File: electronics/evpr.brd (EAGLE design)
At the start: 97.2 x 41.3 mm, 127 parts, among them J1 10118193-0001LF, Q1 AOD4184A, Q2 AOD4184A, T3 MMBT2222A, T5 MMBT2222A, U1 BQ2057TTS, U3 ESP32-WROOM-32D, U6 SN74AHCT125DR, U7 TPSM84824MOLR, U8 LTC4353CMSPBFMSOP-16_MS-M, X1 B3P-VH(LF)(SN), X2 BM02B-PASS-1-TFT(LF)(SN), X3 BM03B-PASS-1-TFT(LF)(SN), X4 BM03B-PASS-1-TFT(LF)(SN), X5 BM04B-PASS-1-TFT(LF)(SN)

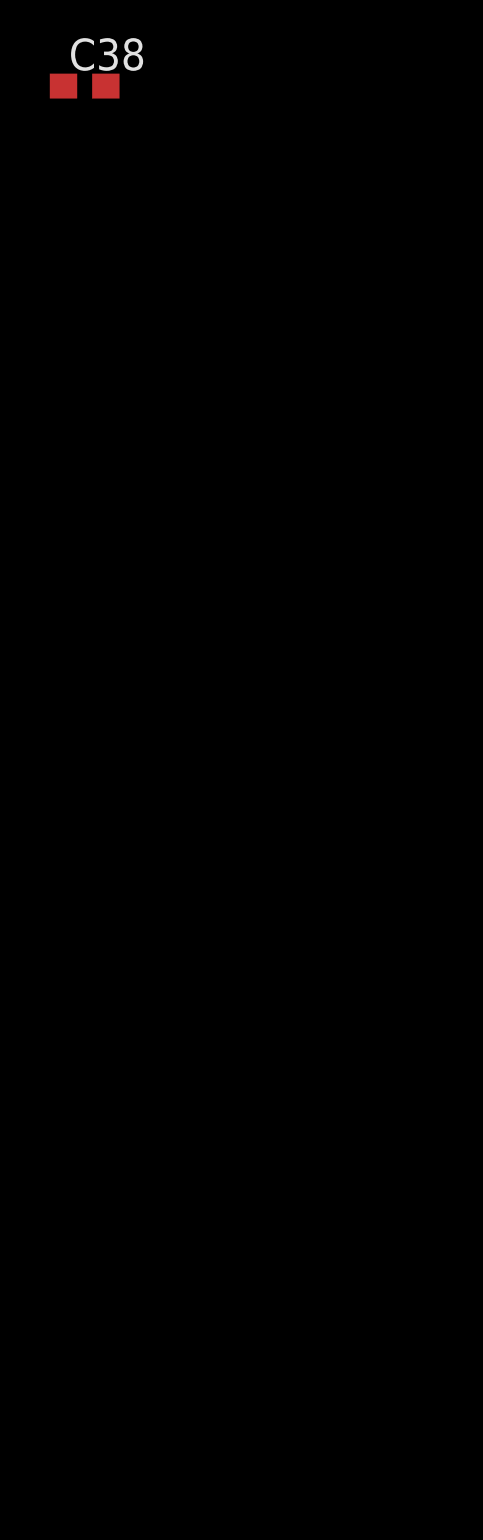
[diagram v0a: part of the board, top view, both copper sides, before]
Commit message: Added EMI Testing optionals
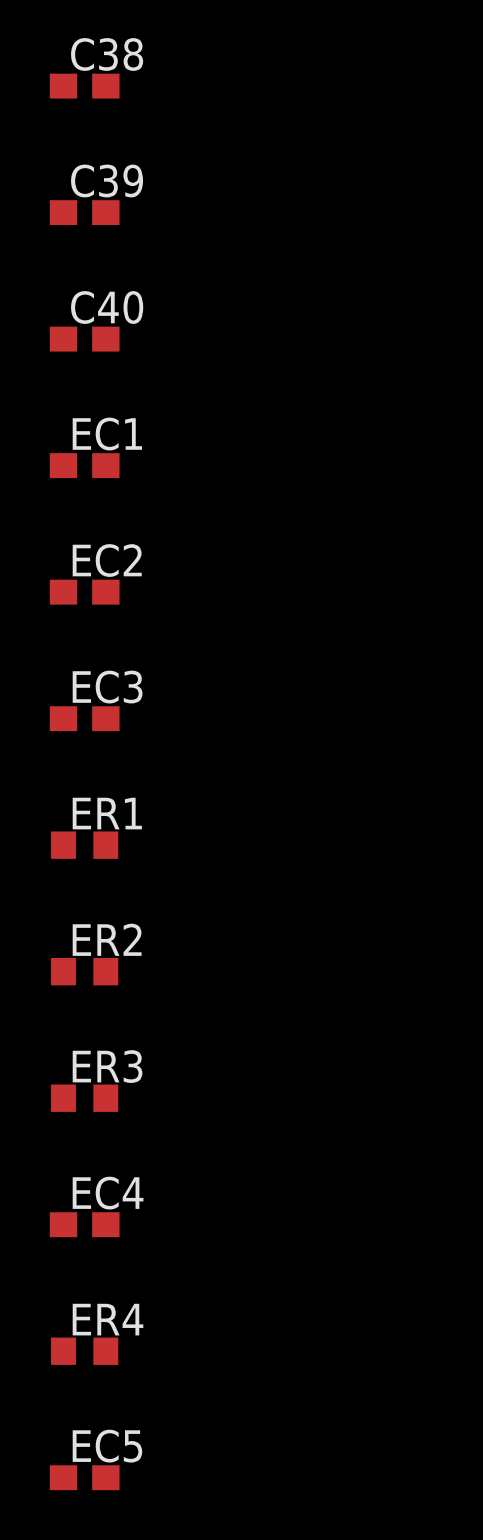
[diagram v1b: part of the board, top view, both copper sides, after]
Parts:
- added C39, C40, EC1, EC2, EC3, EC4, EC5: 0.1uF, eagle-ltspice:C0603
- added ER1, ER2, ER3, ER4: 0, rcl:R0603
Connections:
- new net N$11: ER1.1, X3.P$2
- new net N$12: ER2.1, X4.P$2
- new net N$30: ER3.1, X5.P$2
- new net N$42: ER4.1, X5.P$3
- net ESP_POWER: now also C39.2
- net GND: now also C39.1, C40.2, EC1.2, EC2.2, EC3.2, EC4.2, EC5.2
- net N$22: now also EC4.1, ER4.2; no longer X5.P$3
- net N$27: now also EC5.1, ER3.2; no longer X5.P$2
- net SERVO1: now also EC2.1, ER1.2; no longer X3.P$2
- net SERVO2: now also EC3.1, ER2.2; no longer X4.P$2
- net TACH: now also EC1.1
- net VRAW: now also C40.1

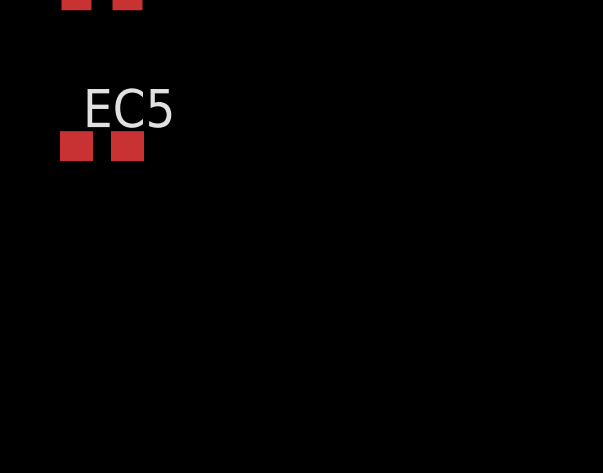
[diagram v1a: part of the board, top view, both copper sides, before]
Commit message: Added testpoints; Reviewed all testpoints; Corrected 3.3V converter to AP63203
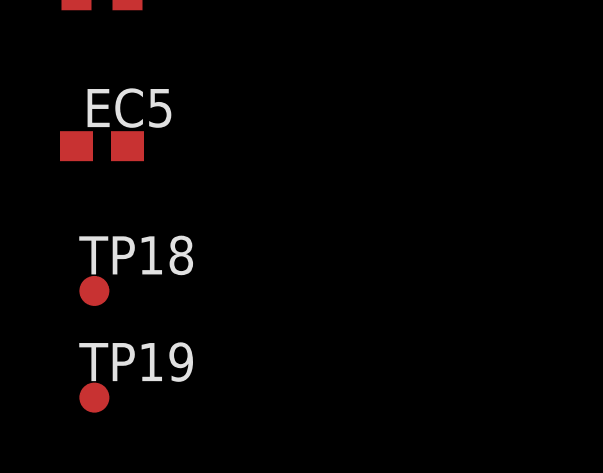
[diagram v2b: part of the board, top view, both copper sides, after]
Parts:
- added TP18, TP19: PTR1TP10R, testpad:TP10R
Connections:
- net N$34: now also TP18.TP
- net N$40: now also TP19.TP
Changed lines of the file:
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@@
 <attribute name="VALUE" x="-73.533" y="-390.779" size="1.27" layer="27"/>
+</element>
+<element name="TP18" library="testpad" library_urn="urn:adsk.eagle:library:385" package="TP10R" package3d_urn="urn:adsk.eagle:package:27959/1" value="PTR1TP10R" x="-73.152" y="-393.7" smashed="yes">
+<attribute name="NAME" x="-73.6521" y="-393.1501" size="1.27" layer="25"/>
+<attribute name="POPULARITY" value="0" x="-73.152" y="-393.7" size="1.778" layer="27" display="off"/>
+<attribute name="TP_SIGNAL_NAME" value="" x="-73.152" y="-393.7" size="1.778" layer="27" display="off"/>
+<attribute name="VALUE" x="-73.533" y="-394.208" size="0.0254" layer="27"/>
+</element>
+<element name="TP19" library="testpad" library_urn="urn:adsk.eagle:library:385" package="TP10R" package3d_urn="urn:adsk.eagle:package:27959/1" value="PTR1TP10R" x="-73.152" y="-397.256" smashed="yes">
+<attribute name="NAME" x="-73.6521" y="-396.7061" size="1.27" layer="25"/>
+<attribute name="POPULARITY" value="0" x="-73.152" y="-397.256" size="1.778" layer="27" display="off"/>
+<attribute name="TP_SIGNAL_NAME" value="" x="-73.152" y="-397.256" size="1.778" layer="27" display="off"/>
+<attribute name="VALUE" x="-73.533" y="-397.764" size="0.0254" layer="27"/>
 </element>
 </elements>
@@
 <wire x1="41.654" y1="-16.002" x2="41.654" y2="-18.352" width="0.254" layer="16"/>
 <wire x1="41.654" y1="-18.352" x2="41.554" y2="-18.452" width="0.254" layer="16"/>
+<contactref element="TP18" pad="TP"/>
+<wire x1="41.656" y1="-21.121" x2="-73.152" y2="-393.7" width="0" layer="19" extent="1-16"/>
 </signal>
 <signal name="N$29">
@@
 <contactref element="C16" pad="2"/>
 <contactref element="C22" pad="2"/>
+<contactref element="TP19" pad="TP"/>
+<wire x1="-61.126" y1="-70.358" x2="-73.152" y2="-397.256" width="0" layer="19" extent="1-1"/>
 <wire x1="-61.126" y1="-65.278" x2="-61.126" y2="-70.358" width="0" layer="19" extent="1-1"/>
 <wire x1="33.635" y1="-29.546" x2="-61.126" y2="-65.278" width="0" layer="19" extent="1-16"/>

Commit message: Update all component names to follow new standard naming system
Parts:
- renumbered C1 to C.M1, C10 to C.M10, C11 to C.Z11, C12 to C.F12, C13 to C.B13, C14 to C.Z14, C15 to C.F15, C16 to C.P16, C17 to C.F17, C18 to C.Z18, C19 to C.Z19, C2 to C.M2, C20 to C.F20, C21 to C.D21, C22 to C.P22, C23 to C.P23, C24 to C.P24, C25 to C.Z25, C26 to C.F26, C27 to C.J27, C28 to C.J28, C29 to C.M29, C3 to C.M3, C30 to C.L30, C31 to C.L31, C32 to C.B32, C33 to C.Y33, C34 to C.Z34, C35 to C.F35, C36 to C.F36, C37 to C.S37, C38 to C.S38, C39 to C.G39, C4 to C.M4, C40 to C.M40, C5 to C.M5, C6 to C.Y6, C7 to C.Y7, C8 to C.Y8, C9 to C.F9, EC1 to C.EJ1, EC2 to C.ES2, EC3 to C.ES3, EC4 to R.CD4, EC5 to R.CD5, ER1 to R.ES1, ER2 to R.ES2, ER3 to R.ED3, ER4 to R.ED4, F1 to F.D1, J1 to X.F1, LED1 to D.J1, LED2 to L.P2, LED3 to D.F3, Q1 to Q.Y1, Q2 to Q.Y2, R1 to R.M1, R10 to R.G10, R11 to R.M11, R12 to R.P12, R13 to R.P13, R14 to R.P14, R15 to R.J15, R16 to R.P16, R17 to R.F17, R18 to R.F18, R19 to R.F19, R20 to R.J20, R21 to R.J21, R22 to R.J22, R23 to R.J23, R24 to R.L24, R25 to R.L25, R26 to R.L26, R27 to R.L27, R28 to R.K28, R3 to R.B3, R30 to R.F30, R32 to R.M32, R33 to R.L33, R34 to R.L34, R4 to R.B4, R5 to R.B5, R6 to R.B6, R7 to R.Y7, R8 to R.M8, R9 to R.K9, SJ2 to SJ.K2, SV5 to X.G1, T3 to T.P3, T5 to T.P5, TP1 to TP.Y1, TP10 to TP.F10, TP11 to TP.F11, TP12 to TP.Z12, TP13 to TP.P13, TP14 to TP.P14, TP15 to TP.P15, TP16 to TP.P16, TP17 to TP.Z17, TP18 to TP.F18, TP19 to TP.P19, TP2 to TP.J2, TP3 to TP.J3, TP4 to TP.L4, TP5 to TP.M5, TP6 to TP.B6, TP7 to TP.M7, TP8 to TP.L8, TP9 to TP.F9, U$1 to X.K1, U$10 to Q.Z10, U$11 to Q.L11, U$12 to U.P12, U$13 to Q.Z13, U$15 to C.D15, U$16 to Q.J16, U$17 to U.Z17, U$19 to L.Z19, U$2 to U.F2, U$20 to L.F20, U$3 to Q.B3, U$4 to Q.K4, U$5 to Q.L5, U$6 to Q.F6, U$7 to Q.F7, U$8 to Q.Z8, U$9 to Q.L9, U1 to U.B1, U3 to U.G3, U6 to U.D6, U8 to U.Y8, X1 to X.J1, X2 to X.S2, X3 to X.S3, X4 to X.S4, X5 to X.D5, XA1 to X.L1, XA2 to X.L2

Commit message: Hacked USB profile to have wires on internal layers. Seems to make Eagle behave.
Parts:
- removed C.ES3: 0.1uF, eagle-ltspice:C0603
- removed R.B5, R.B6: 100k, rcl:R0603
- removed TP.J3: PTR1TP10R, testpad:TP10R
- removed X.S4: BM03B-PASS-1-TFT(LF)(SN), mccloud:BM03B-PASS-1-TFT(LF)(SN)
- added C.ES1: 0.1uF, eagle-ltspice:C0603
- added R.B1: 0.25, rcl:R0603
- added R.B2: 1k, rcl:R0603
- added TP.J1: PTR1TP10R, testpad:TP10R
- added X.S1: BM02B-PASS-1-TFT(LF)(SN), mccloud:BM02B-PASS-1-TFT(LF)(SN)
- R.B3: value 0.25 -> 100k
- R.B4: value 1k -> 100k
- X.S2: value BM02B-PASS-1-TFT(LF)(SN) -> BM03B-PASS-1-TFT(LF)(SN); device mccloud:BM02B-PASS-1-TFT(LF)(SN) -> mccloud:BM03B-PASS-1-TFT(LF)(SN)
- moved X.S3 270.1 mm to (75.9, -27.9)
- moved X.S2 11.2 mm to (-68.3, -256.3)
- moved R.B4 7.43 mm to (-12.9, -45.8), flipped to the bottom, turned to 270 degrees
- moved TP.J2 6.94 mm to (-24.9, -40.6), flipped to the top, turned to 90 degrees
- moved C.ES2 5.08 mm to (-72.9, -358.4)
- moved R.B3 1.73 mm to (-16.5, -45.8), flipped to the bottom, turned to 0 degrees
- renumbered C.B13 to C.B1, C.B32 to C.B2, C.D15 to C.D1, C.D21 to C.D2, C.F12 to C.F2, C.F15 to C.F3, C.F17 to C.F4, C.F20 to C.F5, C.F26 to C.F6, C.F35 to C.F7, C.F36 to C.F8, C.F9 to C.F1, C.G39 to C.G1, C.J27 to C.J1, C.J28 to C.J2, C.L30 to C.L1, C.L31 to C.L2, C.M10 to C.M6, C.M29 to C.M7, C.M40 to C.M8, C.P16 to C.P1, C.P22 to C.P2, C.P23 to C.P3, C.P24 to C.P4, C.S37 to C.S1, C.S38 to C.S2, C.Y33 to C.Y4, C.Y6 to C.Y1, C.Y7 to C.Y2, C.Y8 to C.Y3, C.Z11 to C.Z1, C.Z14 to C.Z2, C.Z18 to C.Z3, C.Z19 to C.Z4, C.Z25 to C.Z5, C.Z34 to C.Z6, D.F3 to D.F1, L.F20 to L.F1, L.P2 to L.P1, L.Z19 to L.Z1, Q.B3 to Q.B1, Q.F6 to Q.F1, Q.F7 to Q.F2, Q.J16 to Q.J1, Q.K4 to Q.K1, Q.L11 to Q.L3, Q.L5 to Q.L1, Q.L9 to Q.L2, Q.Z10 to Q.Z2, Q.Z13 to Q.Z3, Q.Z8 to Q.Z1, R.CD4 to R.CD1, R.CD5 to R.CD2, R.ED3 to R.ED1, R.ED4 to R.ED2, R.F17 to R.F1, R.F18 to R.F2, R.F19 to R.F3, R.F30 to R.F4, R.G10 to R.G1, R.J15 to R.J1, R.J20 to R.J2, R.J21 to R.J3, R.J22 to R.J4, R.J23 to R.J5, R.K28 to R.K2, R.K9 to R.K1, R.L24 to R.L1, R.L25 to R.L2, R.L26 to R.L3, R.L27 to R.L4, R.L33 to R.L5, R.L34 to R.L6, R.M11 to R.M3, R.M32 to R.M4, R.M8 to R.M2, R.P12 to R.P1, R.P13 to R.P2, R.P14 to R.P3, R.P16 to R.P4, R.Y7 to R.Y1, SJ.K2 to SJ.K1, T.P3 to T.P1, T.P5 to T.P2, TP.B6 to TP.B1, TP.F10 to TP.F2, TP.F11 to TP.F3, TP.F18 to TP.F4, TP.F9 to TP.F1, TP.L4 to TP.L1, TP.L8 to TP.L2, TP.M5 to TP.M1, TP.M7 to TP.M2, TP.P13 to TP.P1, TP.P14 to TP.P2, TP.P15 to TP.P3, TP.P16 to TP.P4, TP.P19 to TP.P5, TP.Z12 to TP.Z1, TP.Z17 to TP.Z2, U.D6 to U.D1, U.F2 to U.F1, U.G3 to U.G1, U.P12 to U.P1, U.Y8 to U.Y1, U.Z17 to U.Z1, U7 to U1, X.D5 to X.D1
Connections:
- net GND: now also C.ES1.2, R.B4.1, X.S1.P$1, X.S1.P$5, X.S1.P$6, X.S2.P$3; no longer C.ES3.2, R.B6.1, X.S2.P$1, X.S4.P$3, X.S4.P$5, X.S4.P$6
- net N$11: now also X.S2.P$2; no longer X.S3.P$2
- net N$12: now also X.S3.P$2; no longer X.S4.P$2
- net N$5: now also R.B1.2; no longer R.B3.2
- net N$6: now also R.B2.2; no longer R.B4.2
- net N$7: now also R.B3.1, R.B4.2; no longer R.B5.1, R.B6.2
- net N$9: now also R.B2.1; no longer R.B4.1
- net SERVO1: now also C.ES1.1; no longer C.ES2.1
- net SERVO2: now also C.ES2.1; no longer C.ES3.1
- net SYS_POWER: now also X.S1.P$2, X.S2.P$1; no longer X.S2.P$2, X.S4.P$1
- net TACH_RAW: now also TP.J1.TP; no longer TP.J2.TP
- net VRAW: now also R.B1.1, R.B3.2, TP.J2.TP; no longer R.B3.1, R.B5.2, TP.J3.TP

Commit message: Finished routing board. Wow.
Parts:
- removed C.B2, C.M8, C.S2: 0.1uF, eagle-ltspice:C0603
- removed D.F1, L.P1: (no value), led:CHIP-LED0805
- removed R.F1: 250Ω, rcl:R0603
- removed U1: TPSM84824MOLR, mccloud:MOL0024A
- added D.P1, D.Z1: (no value), led:CHIP-LED0805
- added R.P5: 250Ω, mccloud:R0603
- added U.M1: TPSM84824MOLR, mccloud:MOL0024A
- C.B1, C.D2, C.EJ1, C.ES1, C.ES2, C.F1, C.F2, C.F6, C.F7, C.F8, C.G1, C.J1, C.J2, C.L1, C.L2, C.M7, C.P1, C.P2, C.P3, C.P4, C.S1, C.Y1, C.Y2, C.Y3, C.Y4, C.Z3, C.Z5, C.Z6, R.CD1, R.CD2: device eagle-ltspice:C0603 -> mccloud:C0603
- C.F3, C.F4, C.F5, C.Z2, C.Z4: device rcl:C0603 -> mccloud:C0603
- C.Z1: device eagle-ltspice:C1210 -> mccloud:C0603
- R.B1, R.B2, R.B3, R.B4, R.ED1, R.ED2, R.ES1, R.ES2, R.F2, R.F3, R.F4, R.G1, R.J1, R.J2, R.J3, R.J4, R.J5, R.K1, R.K2, R.L1, R.L2, R.L3, R.L4, R.L5, R.L6, R.M1, R.M2, R.M3, R.M4, R.P1, R.P2, R.P3, R.P4, R.Y1: device rcl:R0603 -> mccloud:R0603
- moved TP.P5 387.5 mm to (30.7, -23.9)
- moved R.CD2 380.5 mm to (39.5, -25.4), flipped to the bottom, turned to 180 degrees
- moved TP.F4 379.1 mm to (45.2, -33.5)
- moved R.ED2 376.4 mm to (37.1, -23.8), turned to 180 degrees
- moved R.CD1 370.0 mm to (38.6, -25.9)
- moved R.ED1 367.9 mm to (39.6, -23.3), flipped to the bottom
- moved R.ES2 345.5 mm to (13.8, -34.1), turned to 120 degrees
- moved R.ES1 337.1 mm to (13.7, -37.6), turned to 300 degrees
- moved C.ES2 333.7 mm to (15.5, -36.7), turned to 300 degrees
- moved C.ES1 326.2 mm to (11.2, -38.1), turned to 300 degrees
- moved C.EJ1 324.8 mm to (-18.8, -27.9), flipped to the bottom, turned to 270 degrees
- moved C.F7 317.8 mm to (46.6, -23.3), turned to 90 degrees
- moved C.F8 314.9 mm to (46.9, -31.6), turned to 90 degrees
- moved C.G1 308.0 mm to (17.7, -43.7), turned to 120 degrees
- moved C.S1 306.2 mm to (8.64, -32.8), turned to 210 degrees
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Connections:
- removed net BUILTIN_LED: R.P4.2
- removed net N$25: D.F1.A, R.F1.1
- removed net SHUTDOWN: U.G1.13
- removed net SHUTDOWN_CANCEL: U.G1.9
- new net N$36: D.Z1.A, R.P5.1
- net 5.0V: no longer R.F1.2
- net AGND: now also U.M1.23, U.M1.3, U.M1.9; no longer U1.23, U1.3, U1.9
- net BATSENSE1: now also U.G1.5; no longer U.G1.4
- net BATSENSE2: now also U.G1.4; no longer U.G1.5
- net ESP_POWER: now also R.P5.2
- net GND: now also D.P1.C, D.Z1.C, U.M1.12, U.M1.13, U.M1.14, U.M1.15, U.M1.18, U.M1.19, U.M1.20, U.M1.21; no longer C.B2.2, C.M8.2, C.S2.1, D.F1.C, L.P1.C, U1.12, U1.13, U1.14, U1.15, U1.18, U1.19, U1.20, U1.21
- net LED_BUILTIN: now also R.P4.2
- net N$11: now also C.ES1.1
- net N$12: now also C.ES2.1
- net N$15: now also U.M1.16, U.M1.17; no longer U1.16, U1.17
- net N$17: now also U.M1.24; no longer U1.24
- net N$24: now also D.P1.A; no longer L.P1.A
- net N$3: now also U.M1.2; no longer U1.2
- net N$31: now also U.M1.5; no longer U1.5
- net POWERSAVE: now also U.G1.33; no longer U.G1.24
- net SERVO1: no longer C.ES1.1
- net SERVO2: no longer C.ES2.1
- net SYS_POWER: no longer C.S2.2
- net USBSENSE: now also U.G1.32; no longer U.G1.23
- net VBAT: no longer C.B2.1
- net VCONV: now also U.M1.1, U.M1.8; no longer U1.1, U1.8
- net VRAW: now also U.M1.11, U.M1.22; no longer C.M8.1, U1.11, U1.22
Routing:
- net RAWSENSE: track 27.6 -> 89.4 mm, vias 2 -> 4
- net SERVO2: track 60.2 -> 3.73 mm
- net VBAT: track 86.3 -> 132.7 mm, vias 11 -> 12
- net SYS_POW_EN: track 18.4 -> 61.4 mm, vias 2 -> 5
- net N$27: track 43.2 -> 4.42 mm, vias 2 -> 0
- net BATSENSE2: track 24.7 -> 63.2 mm, vias 2 -> 6
- net N$22: track 44.0 -> 6.08 mm
- net USING_ENG: track 42.0 -> 77.0 mm, vias 2 -> 5
- net POWERSAVE: track 50.0 -> 84.0 mm, vias 1 -> 5
- net TACH: track 83.3 -> 114.9 mm, vias 2 -> 6
- net CSTAT: track 47.8 -> 77.9 mm, vias 2 -> 5
- net VRAW: track 109.3 -> 81.1 mm, vias 11 -> 12
- net SYS_POWER: track 42.4 -> 70.3 mm, vias 18 -> 25
- net DS_DAT: track 3.73 -> 29.2 mm, vias 1 -> 2
- net BATSENSE1: track 25.3 -> 50.3 mm
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- added copper zone on layer 2, net AGND
- added copper zone on layer 2, net GND
- added copper zone on layer 1, net SYS_POWER
- added copper zone on layer 15, net SYS_POWER
- added copper zone on layer 1, net VBAT
- added copper zone on layer 16, net VBAT
- added copper zone on layer 1, net VCONV
- added copper zone on layer 16, net VCONV
- added copper zone on layer 16, net VRAW
- removed copper zone on layer 15, net GND
- removed copper zone on layer 2, net SYS_POWER
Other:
- board size 97.2 x 41.3 mm -> 88.3 x 47 mm

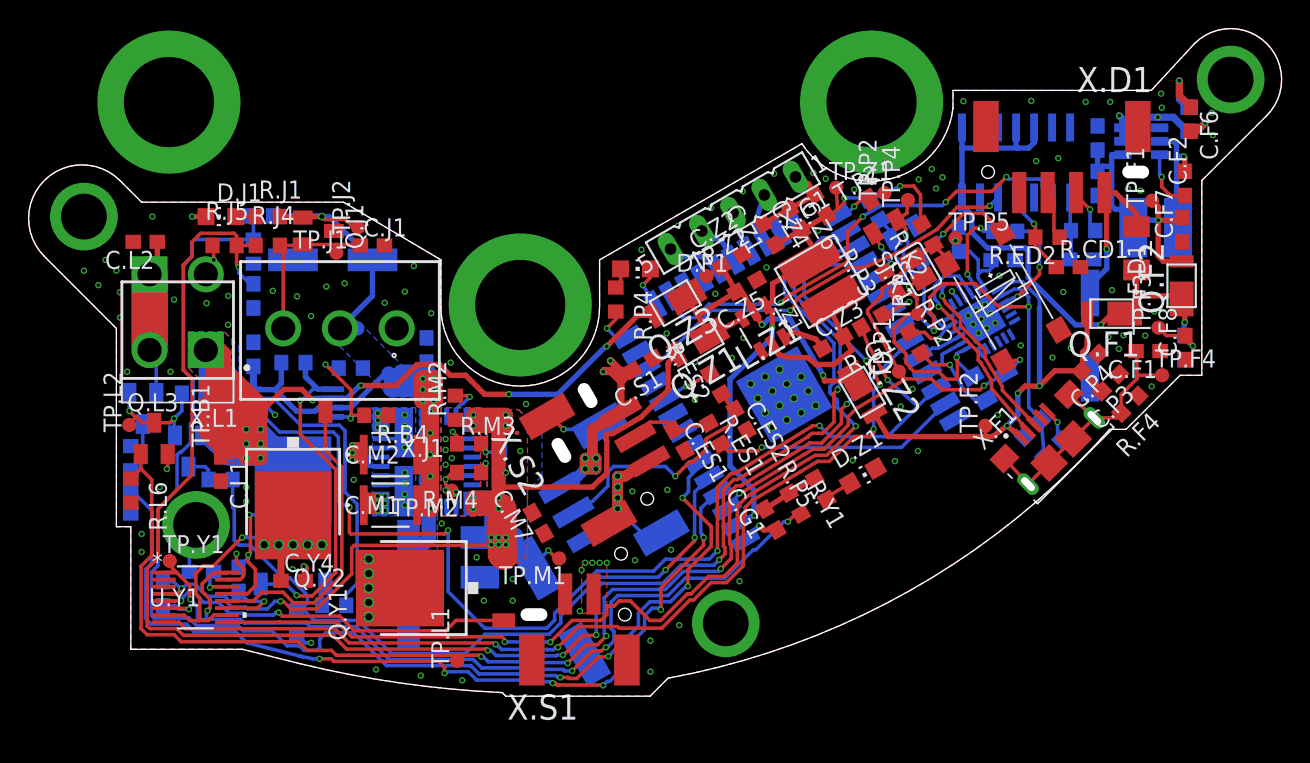
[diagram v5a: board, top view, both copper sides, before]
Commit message: Completed silkscreen alignment
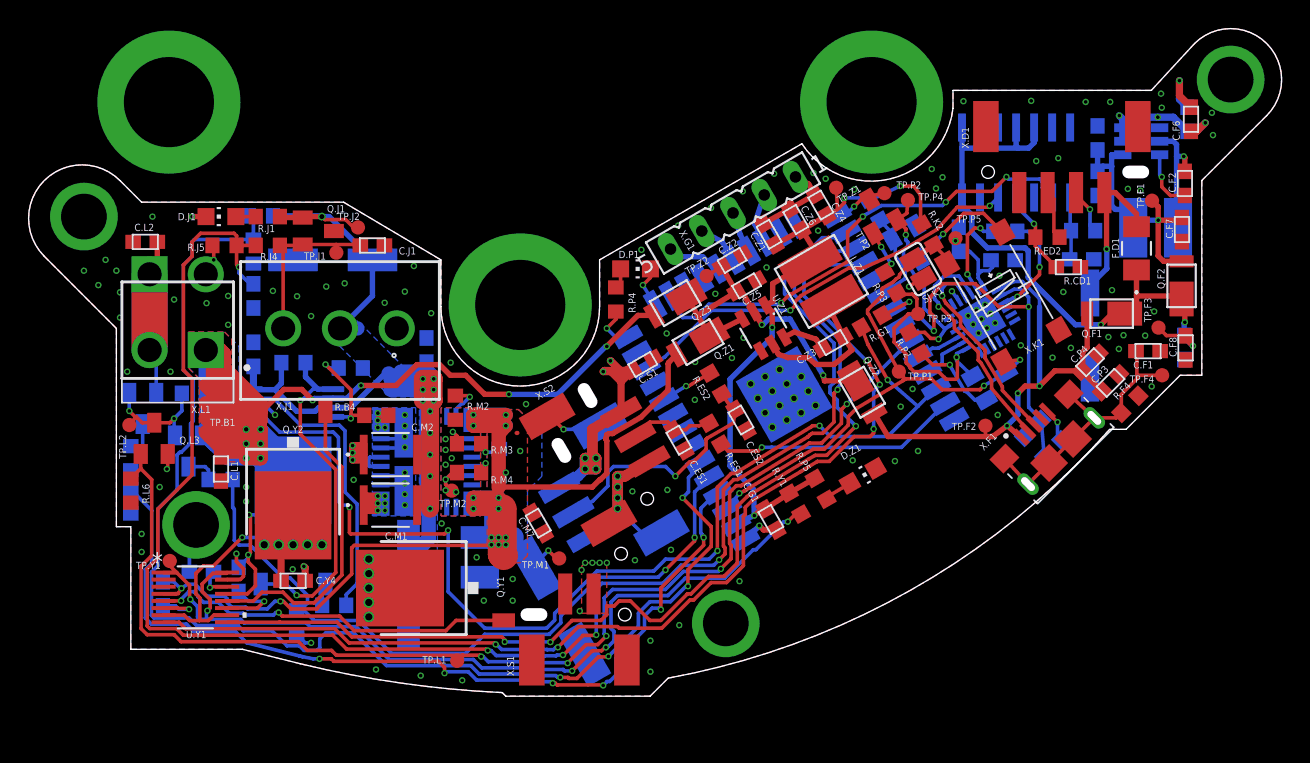
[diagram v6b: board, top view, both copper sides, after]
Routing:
- net GND: vias 165 -> 164

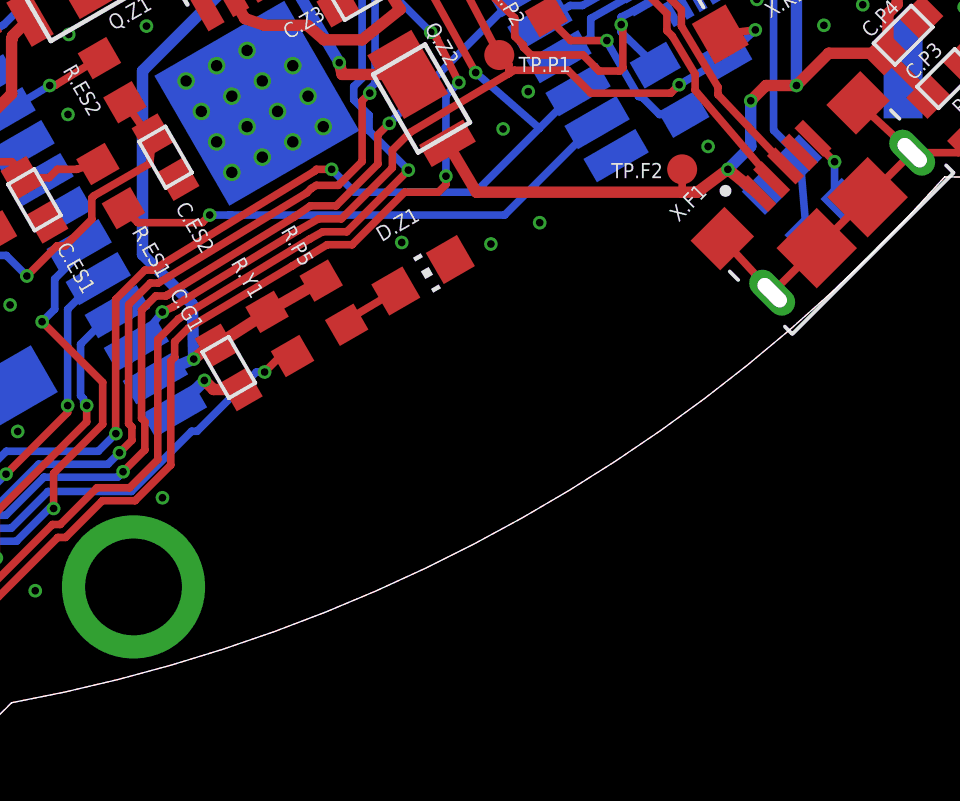
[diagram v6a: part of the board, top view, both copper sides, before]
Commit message: Added logo, board name, credits
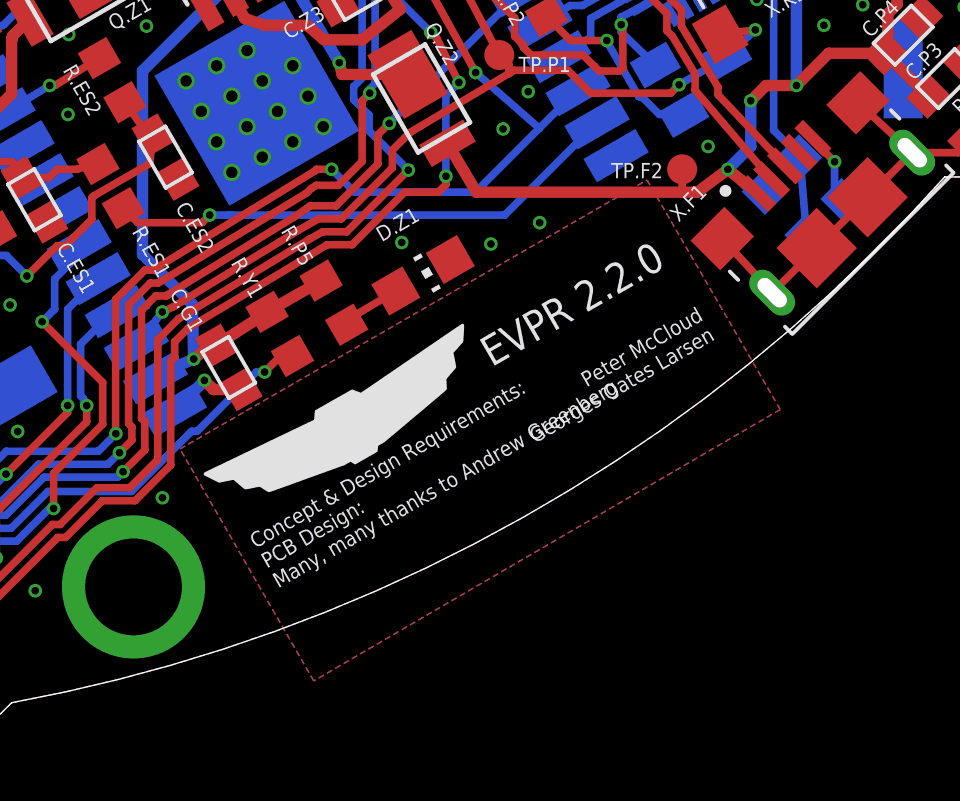
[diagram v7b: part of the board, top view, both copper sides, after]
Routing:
- added copper zone on layer 15, net GND
- added copper zone on layer 2, net SYS_POWER
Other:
- board text added: "Concept & Design Requirements: PCB Design: Many, many thanks to Andrew Greenberg"
- board text added: "EVPR 2.2.0"
- board text added: "Peter McCloud Georges Oates Larsen"
